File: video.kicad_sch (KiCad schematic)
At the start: 75 parts, among them Q10 2N3906, Q4 2N3906, Q5 2N3906, Q6 2N3906, Q7 2N3906, Q8 2N3906, Q9 2N3906

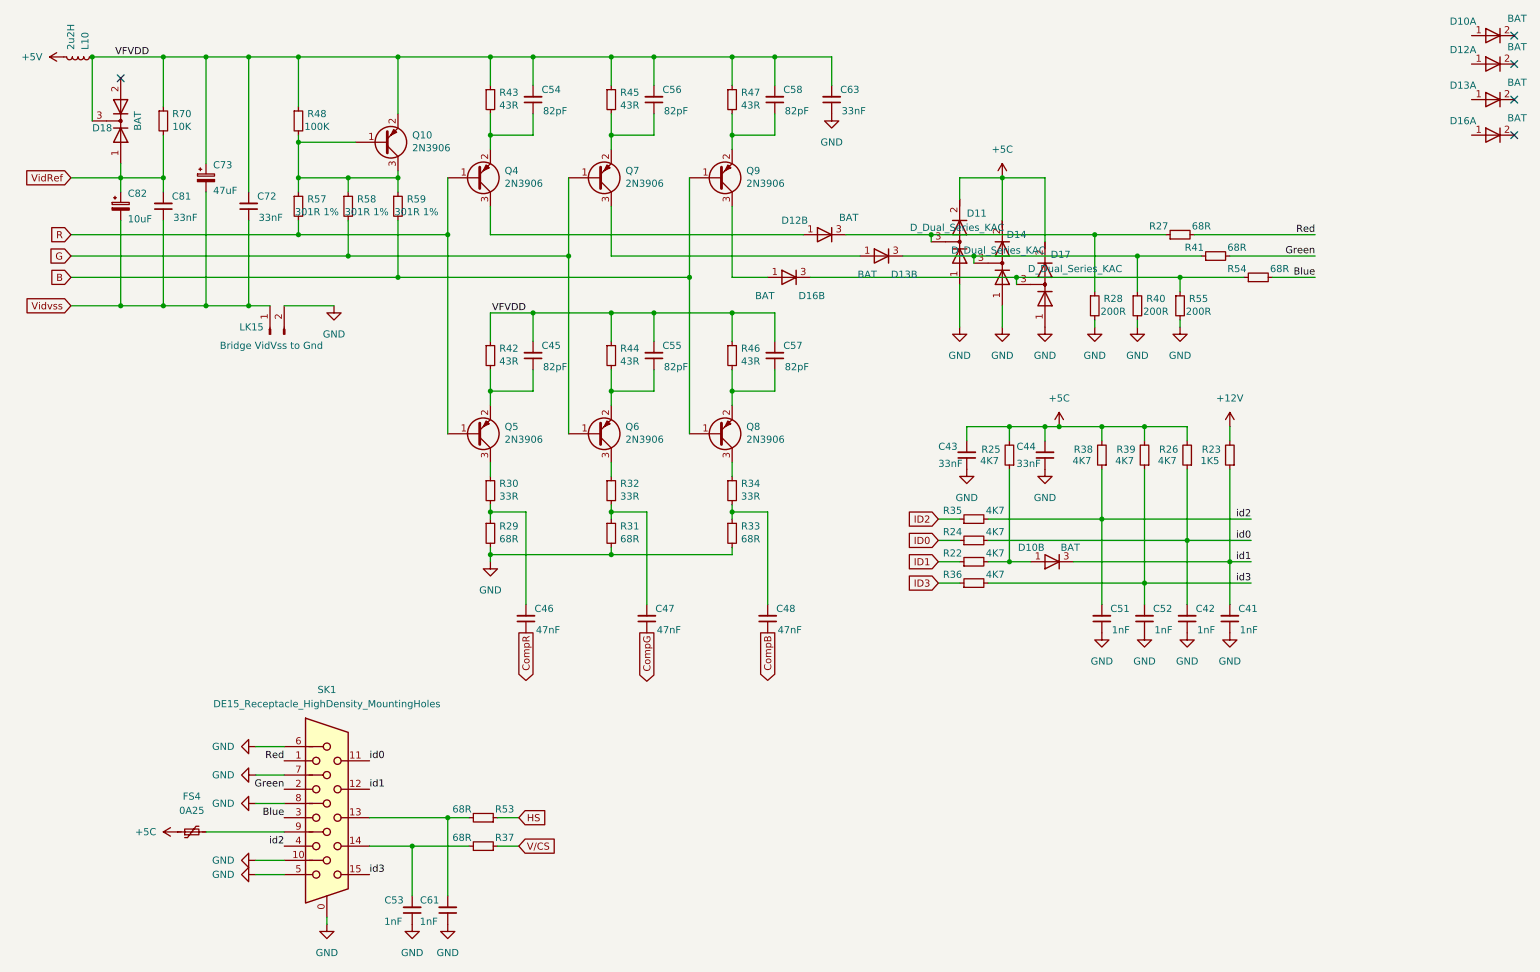
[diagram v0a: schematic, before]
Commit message: adjust shielding perimeter trace and mounting holes
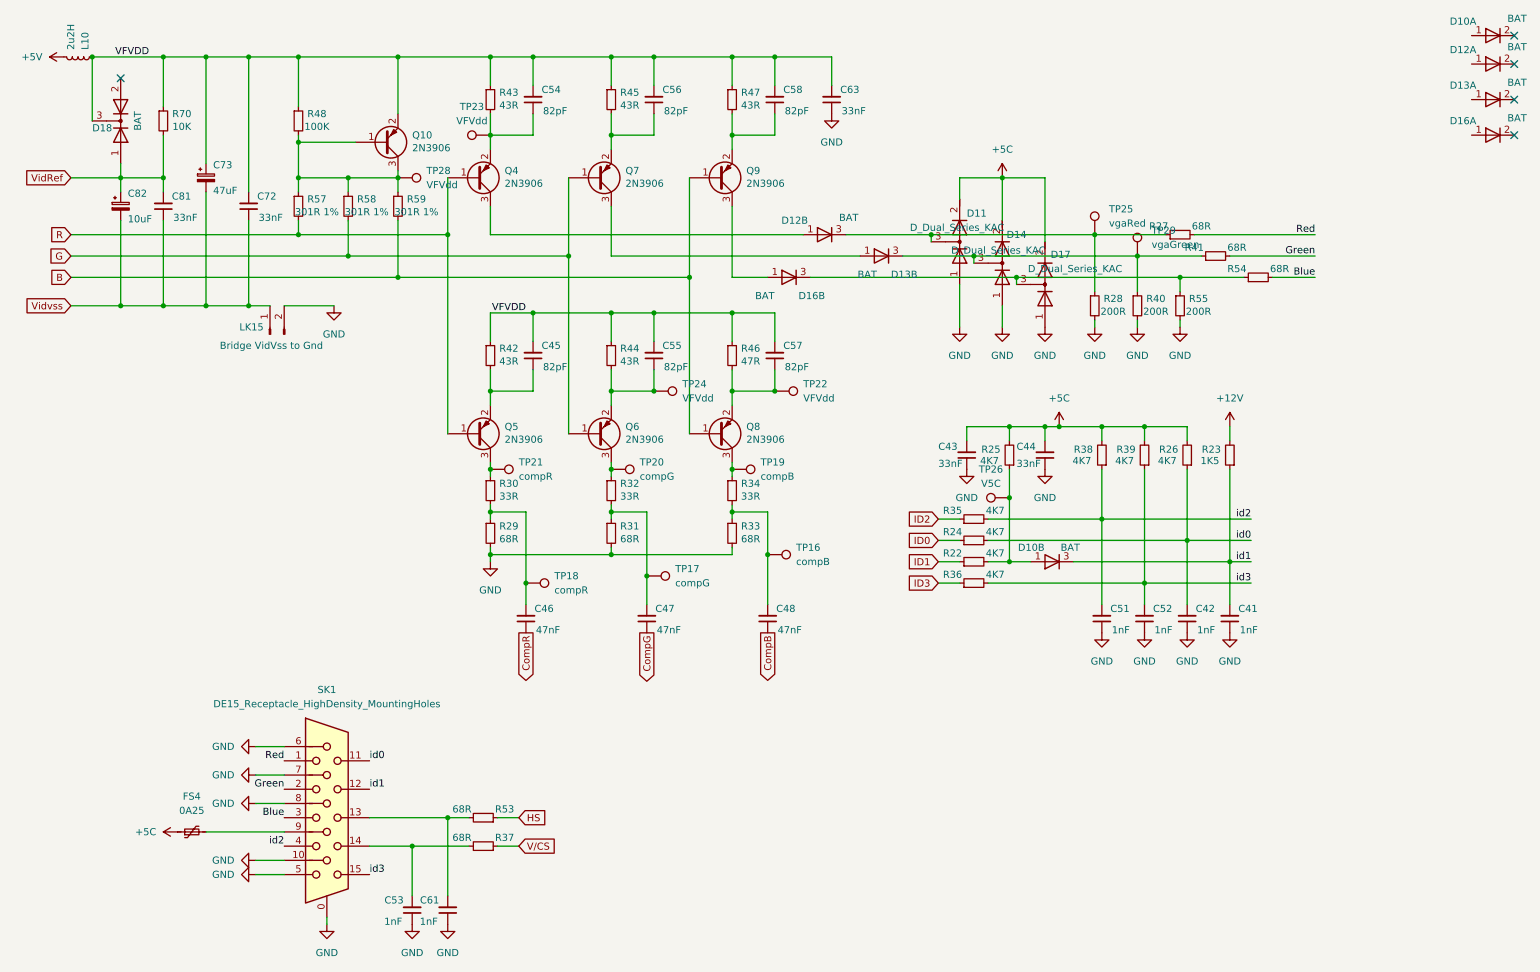
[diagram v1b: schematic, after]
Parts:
- added TP16, TP19: compB, TestPoint:TestPoint_Pad_D1.0mm, symbol Connector:TestPoint
- added TP17, TP20: compG, TestPoint:TestPoint_Pad_D1.0mm, symbol Connector:TestPoint
- added TP18, TP21: compR, TestPoint:TestPoint_Pad_D1.0mm, symbol Connector:TestPoint
- added TP22, TP23, TP24, TP28: VFVdd, TestPoint:TestPoint_Pad_D1.0mm, symbol Connector:TestPoint
- added TP25: vgaRed, TestPoint:TestPoint_Pad_D1.0mm, symbol Connector:TestPoint
- added TP26: V5C, TestPoint:TestPoint_Pad_D1.0mm, symbol Connector:TestPoint
- added TP29: vgaGreen, TestPoint:TestPoint_Pad_D1.0mm, symbol Connector:TestPoint
- R46: value 43R -> 47R
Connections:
- net at C47.2, R31.1, R32.2: now also TP17.1
- net at C55.1, Q6.2 (E), R44.2: now also TP24.1
- net at Q6.3 (C), R32.1: now also TP20.1
- net at D10.1 (A), R22.2, R25.1: now also TP26.1
- net at D11.3 (common), D12.3 (K), R27.1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: now also TP25.1
- net at D13.3 (K), D14.3 (common), R40.1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: now also TP29.1
- net at C48.2, R33.1, R34.2: now also TP16.1
- net at C54.1, Q4.2 (E), R43.2: now also TP23.1
- net at C46.2, R29.1, R30.2: now also TP18.1
- net at C57.1, Q8.2 (E), R46.2: now also TP22.1
- net at Q8.3 (C), R34.1: now also TP19.1
- net at Q10.1 (B), Q10.3 (C), R48.2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: now also TP28.1
- net at Q5.3 (C), R30.1: now also TP21.1

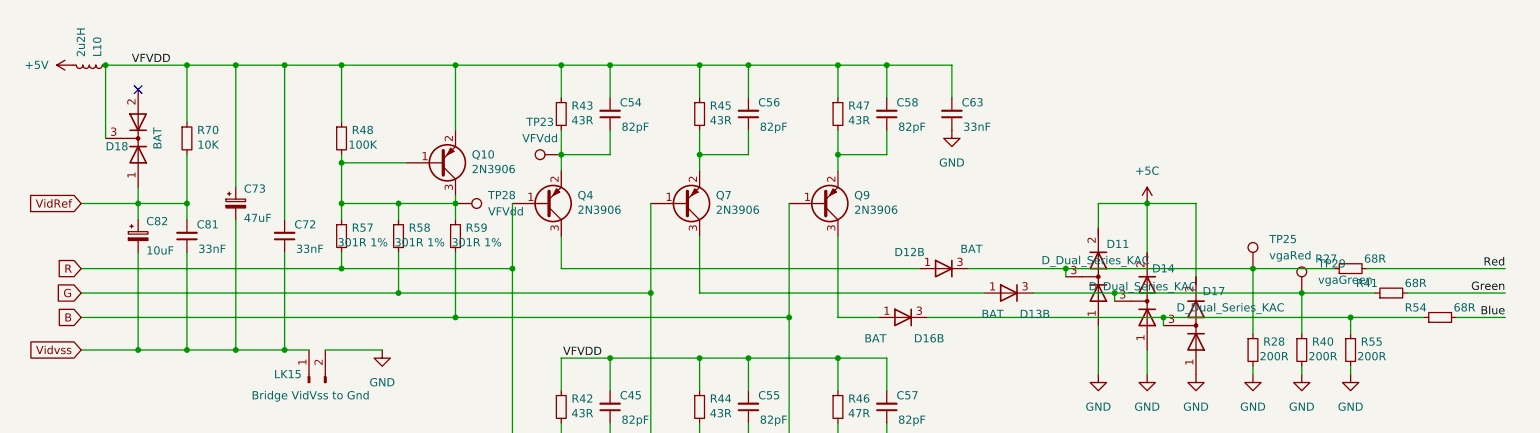
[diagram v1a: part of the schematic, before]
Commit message: add ide and rework onboard ram
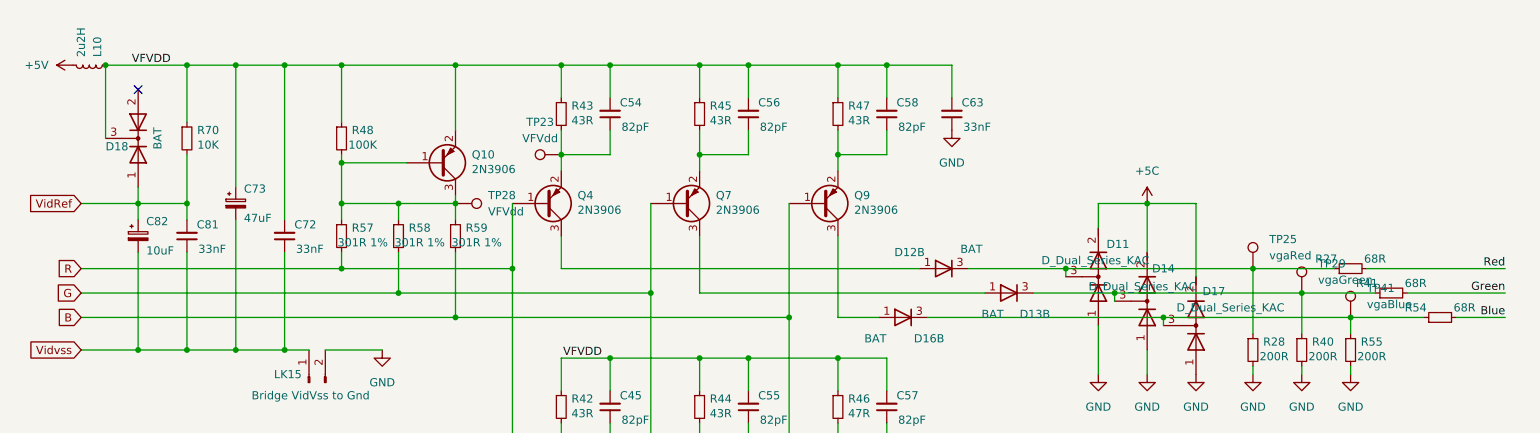
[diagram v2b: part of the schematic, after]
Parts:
- added TP41: vgaBlue, TestPoint:TestPoint_Pad_D1.0mm, symbol Connector:TestPoint
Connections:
- net at D16.3 (K), D17.3 (common), R54.1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: now also TP41.1
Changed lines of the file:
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@@
 (kicad_sch
-	(version 20231120)
+	(version 20250114)
 	(generator "eeschema")
-	(generator_version "8.0")
+	(generator_version "9.0")
 	(paper "A4")
 	(junction
@@
 		)
 		(instances
-			(project ""
+			(project "Acorn-A3010"
 				(path "/999882f3-94f8-4a89-9093-27a47d0cb289/21031065-42cd-49d4-b299-d2e76b62bbd8"
 					(reference "D11")
@@
 		)
 		(instances
-			(project ""
+			(project "Acorn-A3010"
 				(path "/999882f3-94f8-4a89-9093-27a47d0cb289/21031065-42cd-49d4-b299-d2e76b62bbd8"
 					(reference "SK1")
@@
 	)
 	(symbol
+		(lib_id "Connector:TestPoint")
+		(at 220.98 58.42 0)
+		(unit 1)
+		(exclude_from_sim no)
+		(in_bom yes)
+		(on_board yes)
+		(dnp no)
+		(fields_autoplaced yes)
+		(property "Reference" "TP41"
+			(at 223.52 53.8479 0)
+			(effects
+				(font
+					(size 1.27 1.27)
+				)
+				(justify left)
+			)
+		)
+		(property "Value" "vgaBlue"
+			(at 223.52 56.3879 0)
+			(effects
+				(font
+					(size 1.27 1.27)
+				)
+				(justify left)
+			)
+		)
+		(property "Footprint" "TestPoint:TestPoint_Pad_D1.0mm"
+			(at 226.06 58.42 0)
+			(effects
+				(font
+					(size 1.27 1.27)
+				)
+				(hide yes)
+			)
+		)
+		(property "Datasheet" "~"
+			(at 226.06 58.42 0)
+			(effects
+				(font
+					(size 1.27 1.27)
+				)
+				(hide yes)
+			)
+		)
+		(property "Description" "test point"
+			(at 220.98 58.42 0)
+			(effects
+				(font
+					(size 1.27 1.27)
+				)
+				(hide yes)
+			)
+		)
+		(pin "1"
+		)
+		(instances
+			(project "Acorn-A3010"
+				(path "/999882f3-94f8-4a89-9093-27a47d0cb289/21031065-42cd-49d4-b299-d2e76b62bbd8"
+					(reference "TP41")
+					(unit 1)
+				)
+			)
+		)
+	)
+	(symbol
 		(lib_id "Device:R_Small")
 		(at 96.52 154.94 270)
@@
 		)
 		(instances
-			(project ""
+			(project "Acorn-A3010"
 				(path "/999882f3-94f8-4a89-9093-27a47d0cb289/21031065-42cd-49d4-b299-d2e76b62bbd8"
 					(reference "Q5")
@@
 		)
 		(instances
-			(project ""
+			(project "Acorn-A3010"
 				(path "/999882f3-94f8-4a89-9093-27a47d0cb289/21031065-42cd-49d4-b299-d2e76b62bbd8"
 					(reference "#PWR0221")
